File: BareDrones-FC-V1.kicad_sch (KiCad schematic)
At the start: 6 parts

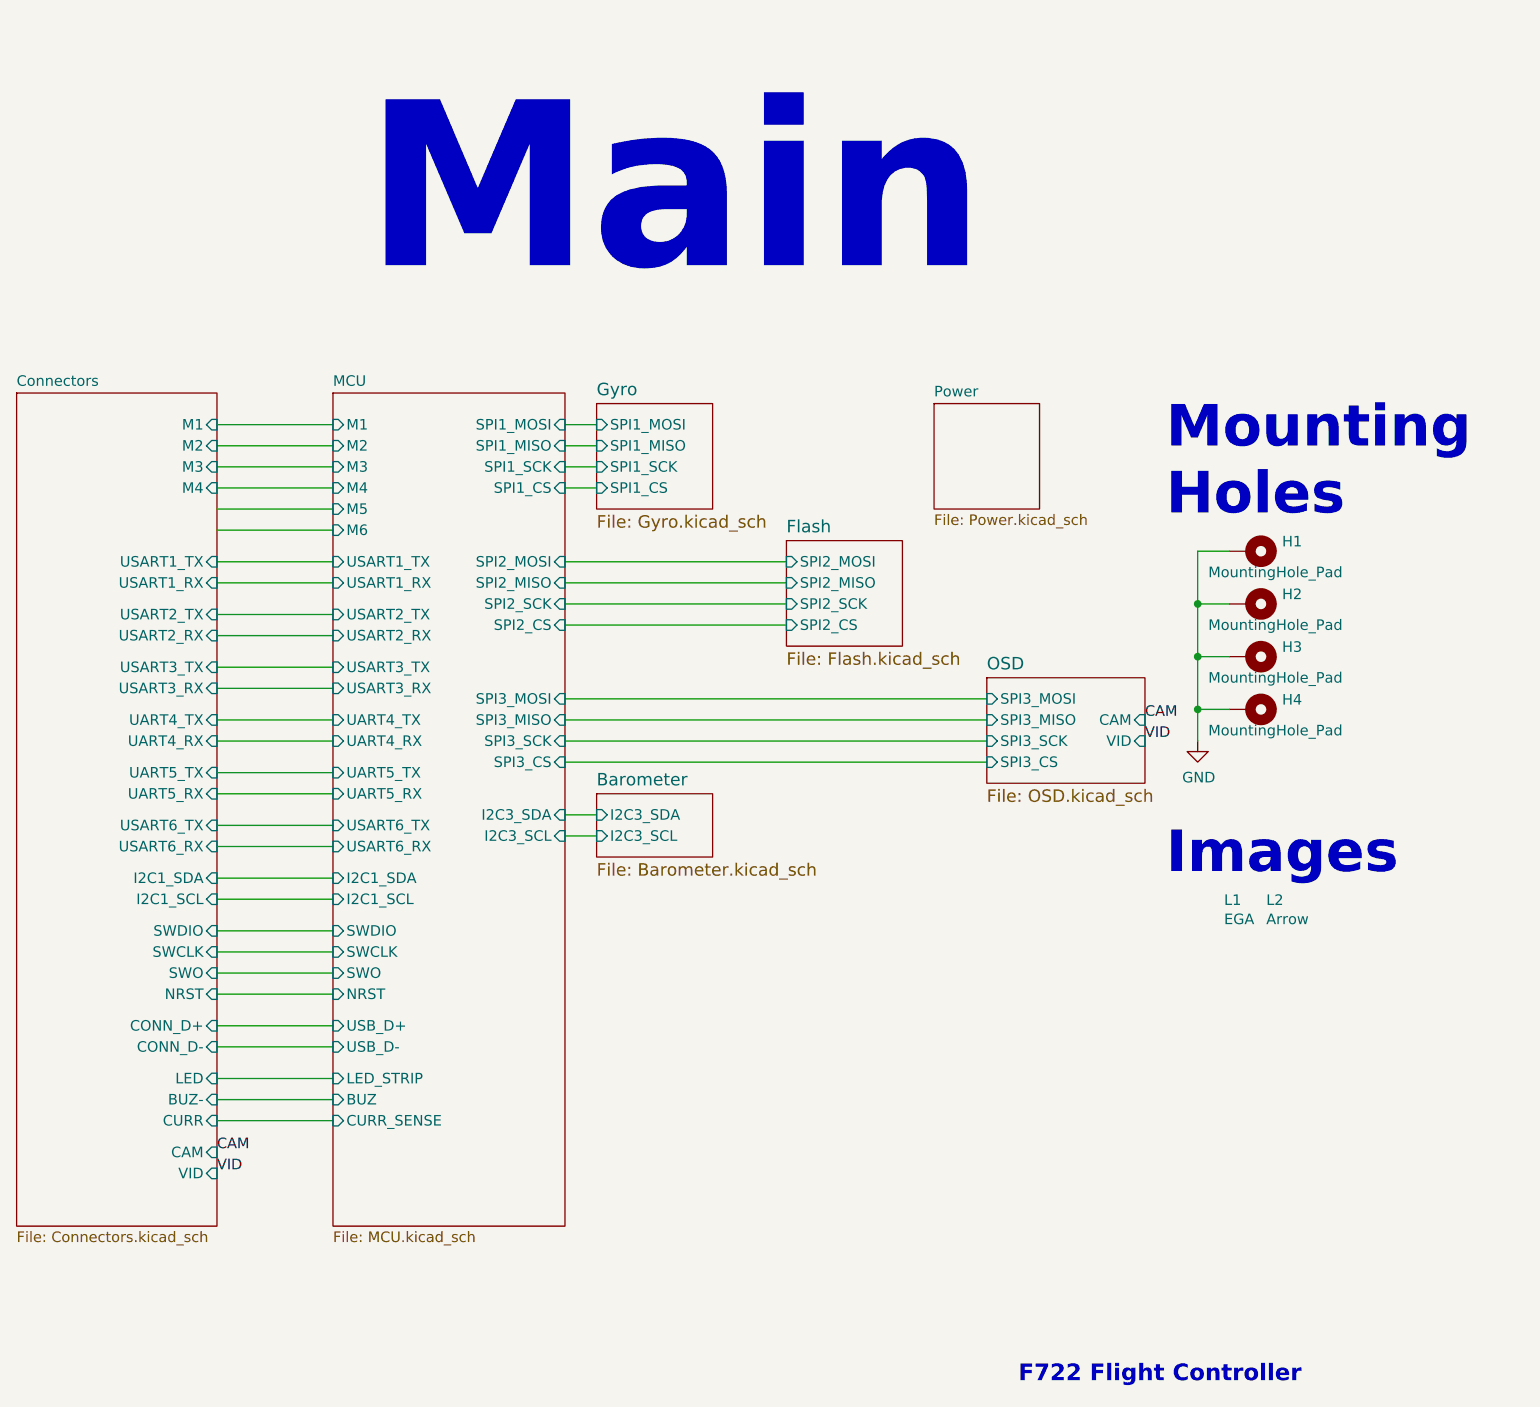
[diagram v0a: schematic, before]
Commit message: Finished power and signal routing.
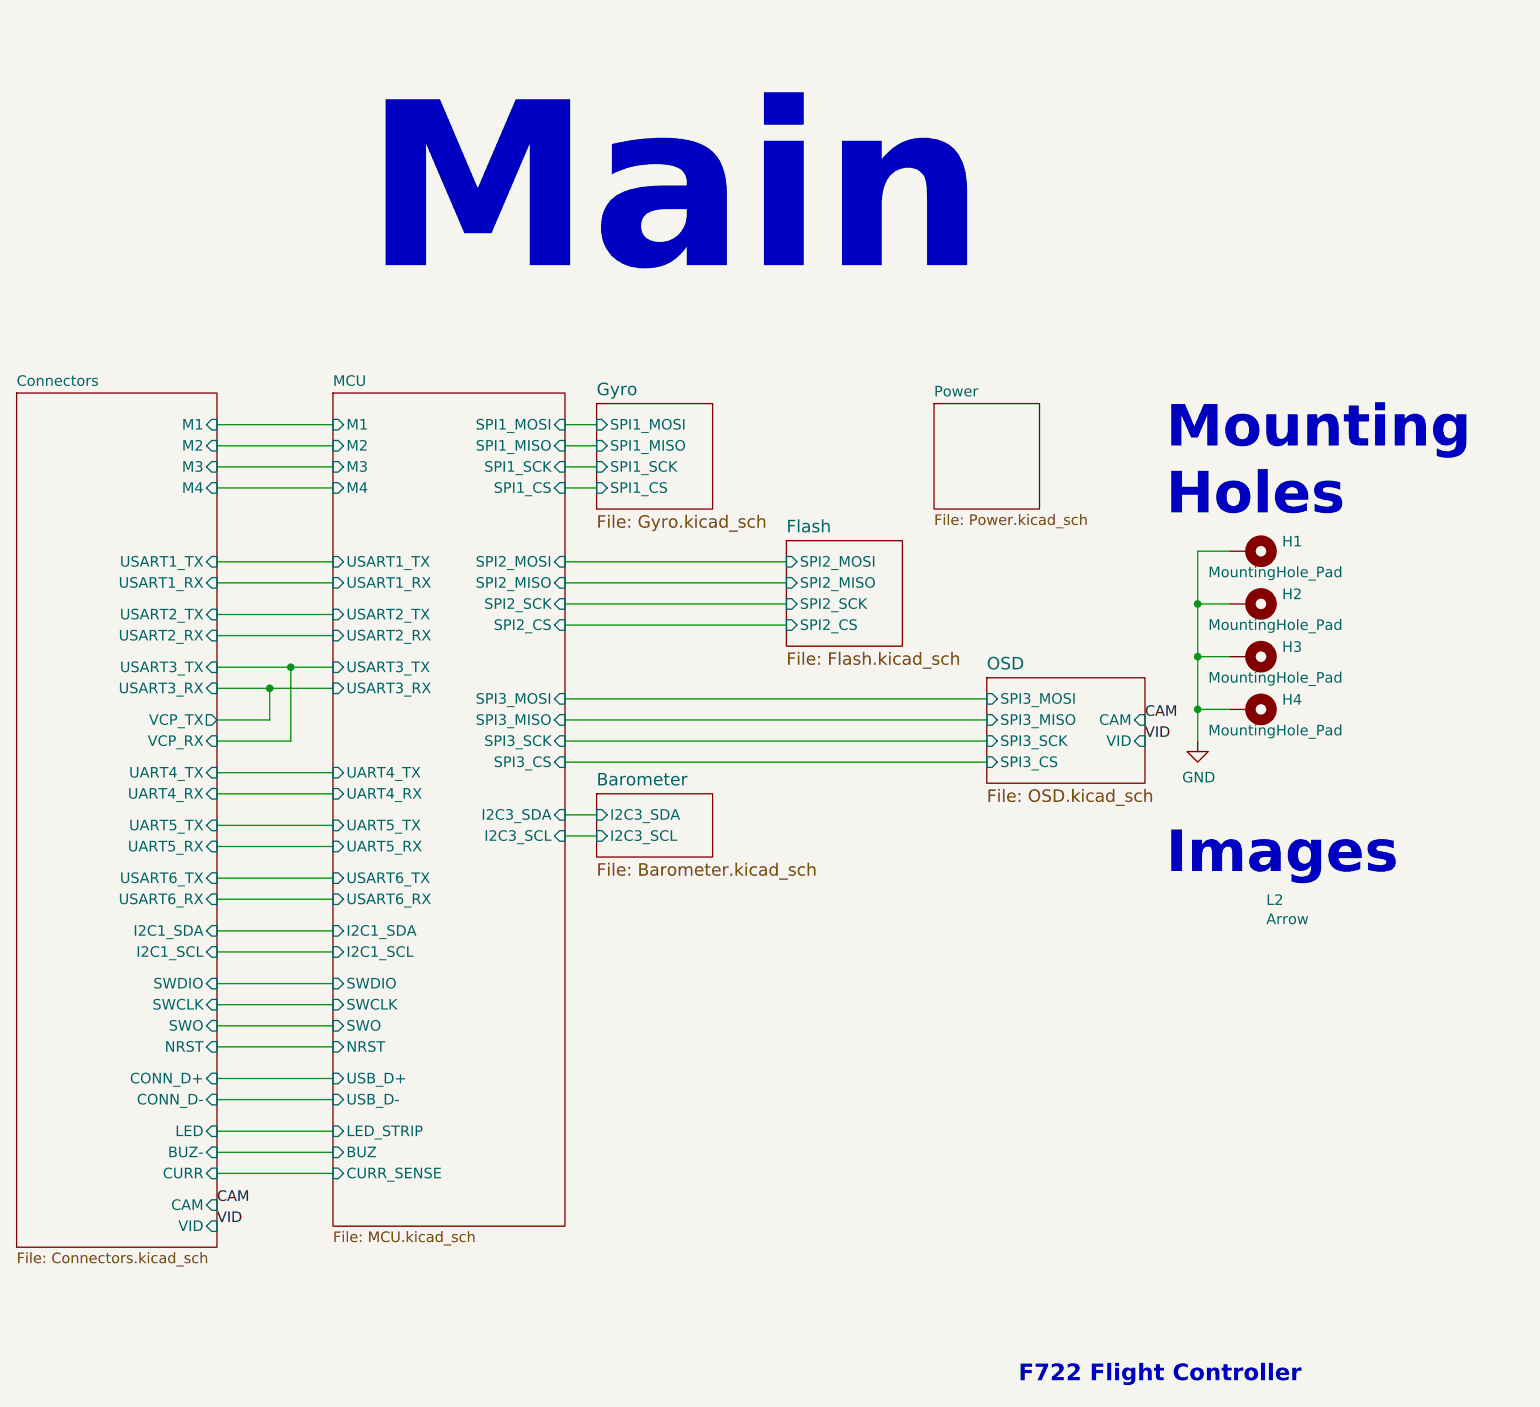
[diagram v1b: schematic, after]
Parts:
- L1: footprint Footprints:EGA -> JPW_Footprints:EGA
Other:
- sheet Connectors ports: added VCP_RX, VCP_TX; removed none
- sheet MCU ports: added none; removed M5, M6
